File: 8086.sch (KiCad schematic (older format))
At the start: 11 parts

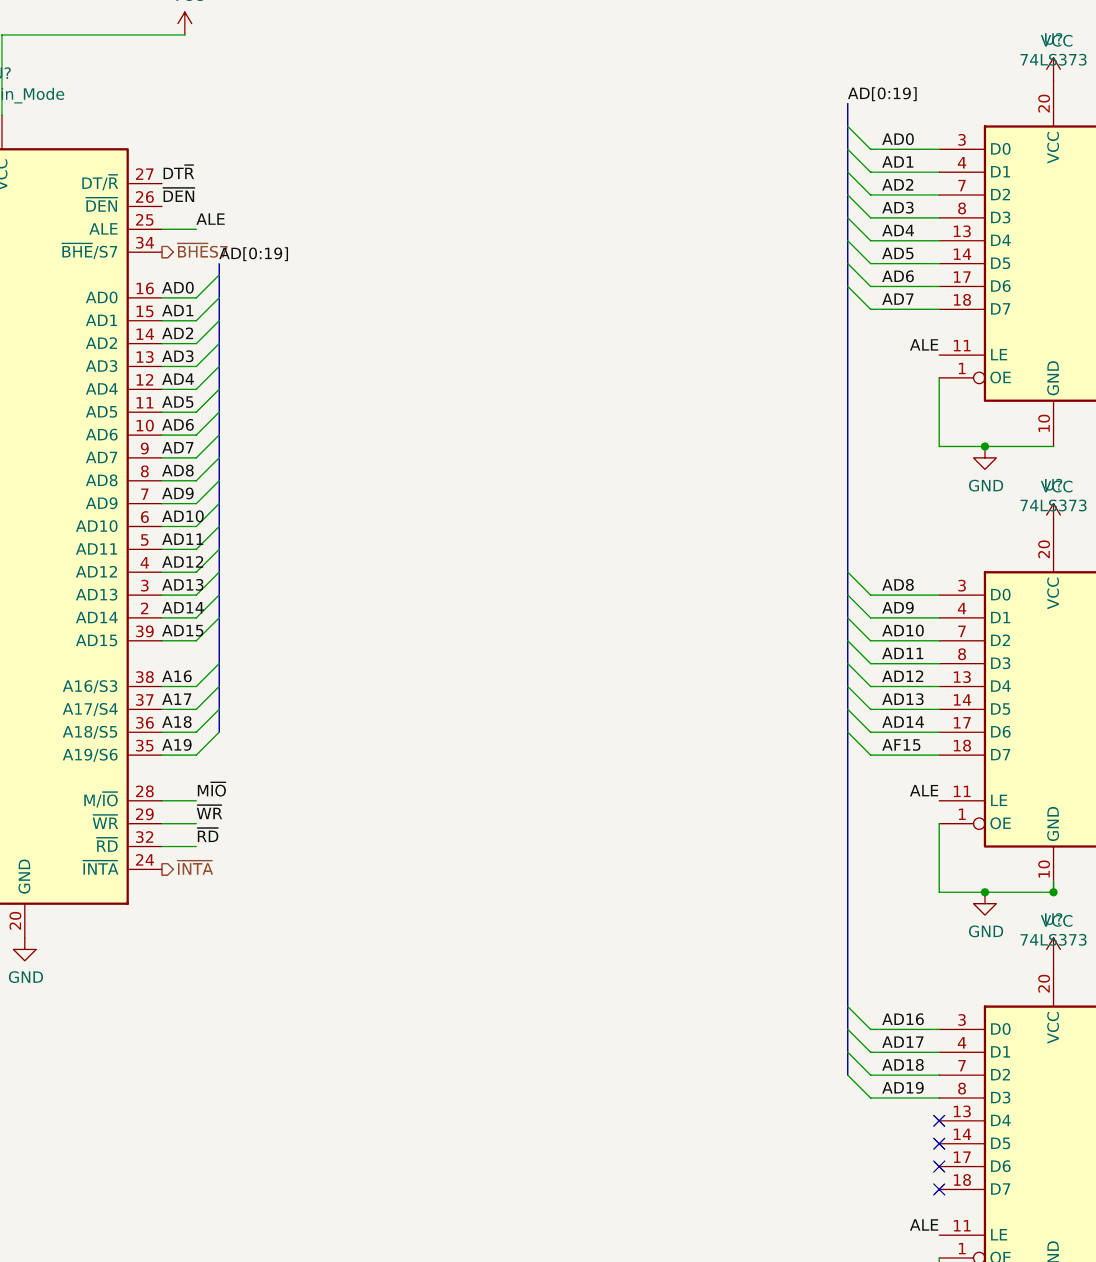
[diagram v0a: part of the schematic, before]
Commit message: Fixed some spelling mistakes
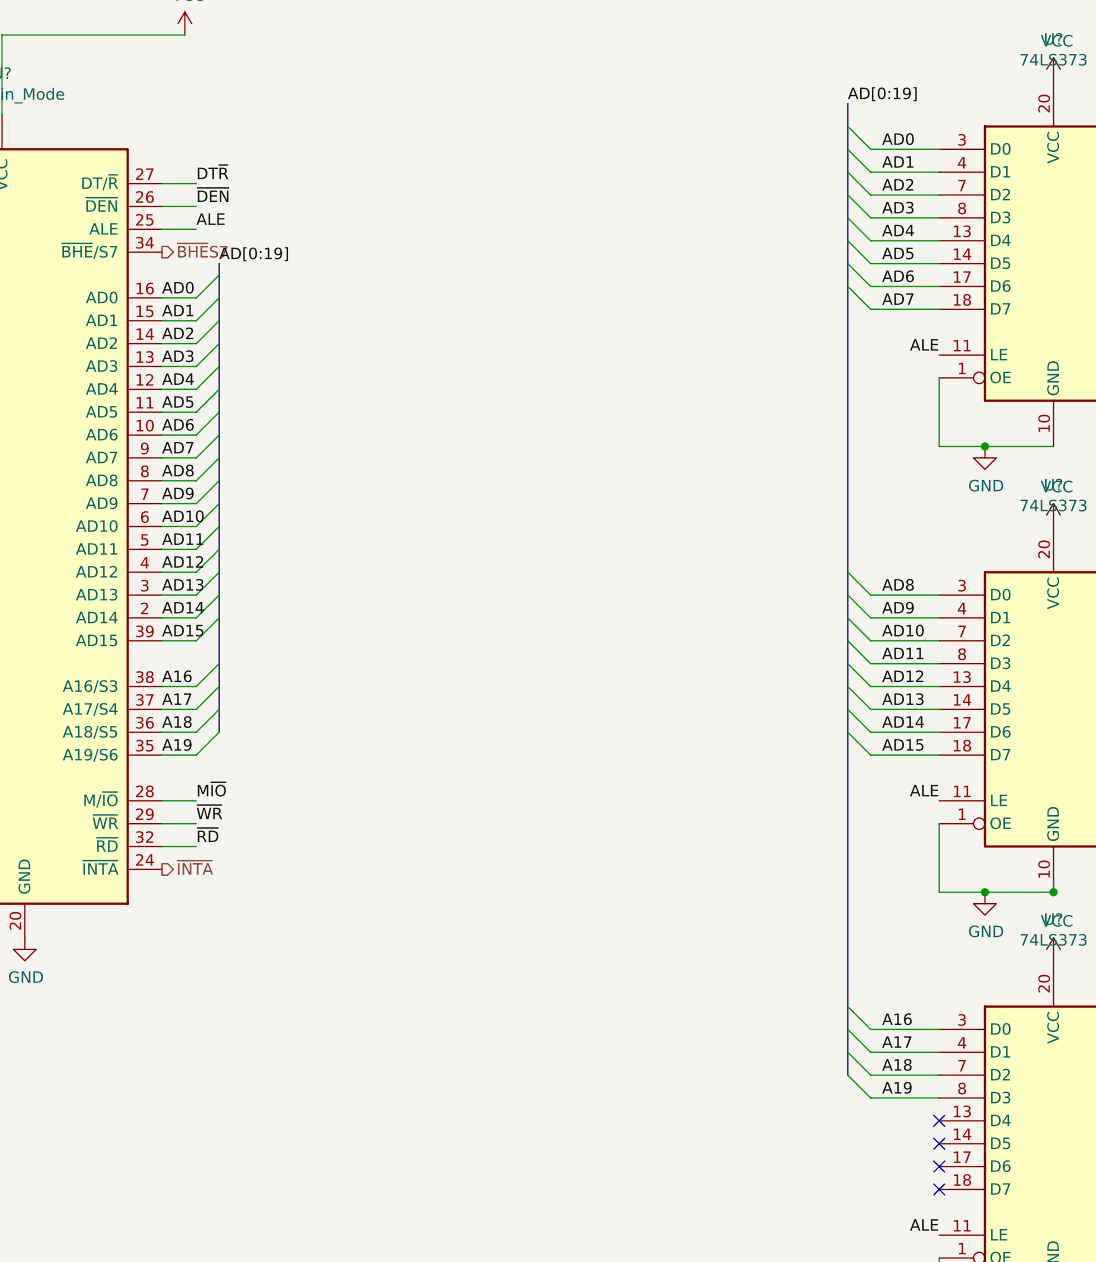
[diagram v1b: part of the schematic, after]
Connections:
- net AD16 is gone; now on net A16: U?.3 (D0)
- net AD17 is gone; now on net A17: U?.4 (D1)
- net AD18 is gone; now on net A18: U?.7 (D2)
- net AD19 is gone; now on net A19: U?.8 (D3)
- net AF15 is gone; now on net AD15: U?.18 (D7)
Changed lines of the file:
@@
 $Descr A4 11693 8268
 encoding utf-8
-Sheet 1 1
+Sheet 1 2
 Title ""
 Date ""
@@
 Wire Wire Line
 	3850 2100 4000 2100
-$Comp
-L MCU_Intel:8086_Min_Mode U?
-U 1 1 60761E58
-P 3150 2700
-F 0 "U?" H 3150 4681 50  0000 C CNN
-F 1 "8086_Min_Mode" H 3150 4590 50  0000 C CNN
-F 2 "Package_DIP:DIP-40_W15.24mm" H 3200 2800 50  0001 C CIN
-F 3 "http://datasheets.chipdb.org/Intel/x86/808x/datashts/8086/231455-006.pdf" H 3150 2750 50  0001 C CNN
-	1    3150 2700
-	1    0    0    -1
-$EndComp
 Wire Wire Line
 	3850 2200 4000 2200
@@
 $EndComp
 Wire Wire Line
-	1850 1900 2450 1900
-Wire Wire Line
 	1850 1550 1850 1900
 Connection ~ 1850 1900
@@
 AD14
 Text Label 7000 3700 0    50   ~ 0
-AF15
+AD15
 Entry Wire Line
 	6850 4800 6950 4900
 Text Label 7000 4900 0    50   ~ 0
-AD16
+A16
 Entry Wire Line
 	6850 4900 6950 5000
 Text Label 7000 5000 0    50   ~ 0
-AD17
+A17
 Entry Wire Line
 	6850 5000 6950 5100
 Text Label 7000 5100 0    50   ~ 0
-AD18
+A18
 Entry Wire Line
 	6850 5100 6950 5200
 Text Label 7000 5200 0    50   ~ 0
-AD19
+A19
 NoConn ~ 7250 5300
 NoConn ~ 7250 5400
@@
 Text Label 9250 2850 0    50   ~ 0
 AD[0:15]
-Text Label 3850 1200 0    50   ~ 0
-DT~R
-Text Label 3850 1300 0    50   ~ 0
+Text Label 4000 1300 0    50   ~ 0
 ~DEN
 Text Label 9650 4050 2    50   ~ 0
@@
 Text HLabel 3850 1500 2    50   Output ~ 0
 ~BHE~S7
-Wire Wire Line
-	2450 1400 2300 1400
 Text Label 2300 1400 2    50   ~ 0
 READY
-Wire Wire Line
-	2300 1600 2450 1600
-Wire Wire Line
-	2450 1200 2300 1200
 $Comp
 L power:GND #PWR?
@@
 	1    0    0    -1
 $EndComp
+Wire Wire Line
+	1850 1900 2450 1900
+Wire Wire Line
+	2300 1600 2450 1600
+Wire Wire Line
+	2450 1400 2300 1400
+Wire Wire Line
+	2450 1200 2300 1200
+$Comp
+L MCU_Intel:8086_Min_Mode U?
+U 1 1 60761E58
+P 3150 2700
+F 0 "U?" H 3150 4681 50  0000 C CNN
+F 1 "8086_Min_Mode" H 3150 4590 50  0000 C CNN
+F 2 "Package_DIP:DIP-40_W15.24mm" H 3200 2800 50  0001 C CIN
+F 3 "http://datasheets.chipdb.org/Intel/x86/808x/datashts/8086/231455-006.pdf" H 3150 2750 50  0001 C CNN
+	1    3150 2700
+	1    0    0    -1
+$EndComp
+Wire Wire Line
+	3850 1200 4000 1200
+Text Label 4000 1200 0    50   ~ 0
+DT~R
+Wire Wire Line
+	3850 1300 4000 1300
+Wire Bus Line
+	9250 2850 9250 5500
 Wire Bus Line
 	6850 850  6850 5100
 Wire Bus Line
 	4100 1550 4100 3600
-Wire Bus Line
-	9250 2850 9250 5500
 $EndSCHEMATC

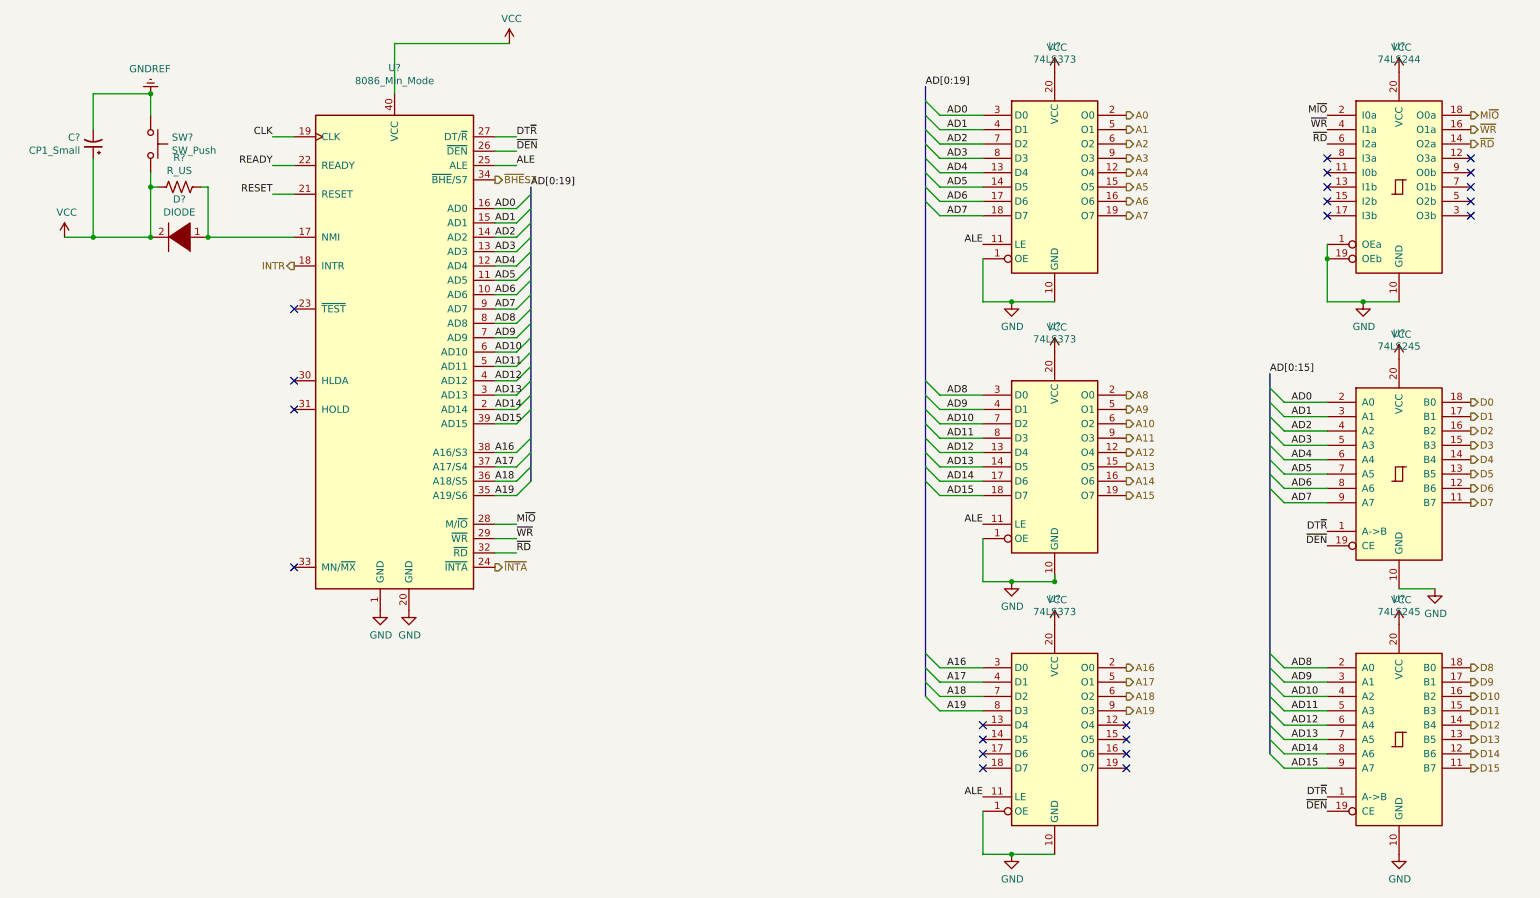
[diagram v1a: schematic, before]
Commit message: Fixed Labels
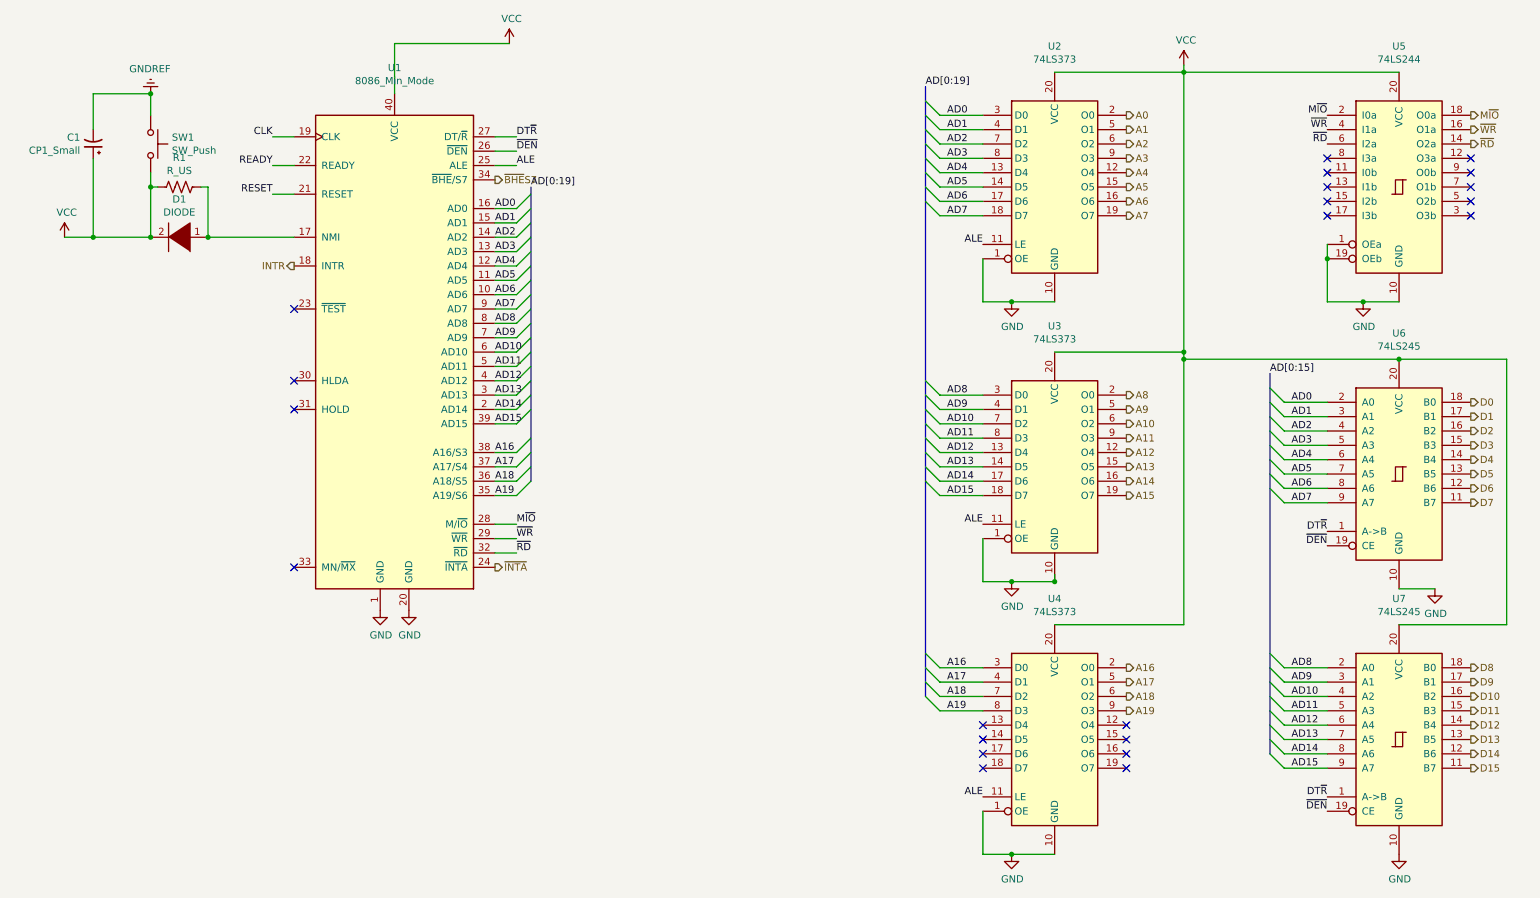
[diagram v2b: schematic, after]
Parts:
- gave numbers to parts that had none: 11
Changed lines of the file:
@@
 $Descr A4 11693 8268
 encoding utf-8
-Sheet 1 2
+Sheet 1 1
 Title ""
 Date ""
@@
 $EndDescr
 $Comp
-L Switch:SW_Push SW?
+L Switch:SW_Push SW1
 U 1 1 607622DA
 P 1450 1250
-F 0 "SW?" V 1404 1398 50  0000 L CNN
+F 0 "SW1" V 1404 1398 50  0000 L CNN
 F 1 "SW_Push" V 1495 1398 50  0000 L CNN
 F 2 "" H 1450 1450 50  0001 C CNN
@@
 	3150 550  3950 550
 $Comp
-L power:VCC #PWR?
+L power:VCC #PWR0101
 U 1 1 60762F72
 P 3950 550
-F 0 "#PWR?" H 3950 400 50  0001 C CNN
+F 0 "#PWR0101" H 3950 400 50  0001 C CNN
 F 1 "VCC" H 3965 723 50  0000 C CNN
 F 2 "" H 3950 550 50  0001 C CNN
@@
 	1450 1550 1500 1550
 $Comp
-L power:VCC #PWR?
+L power:VCC #PWR0102
 U 1 1 60778894
 P 850 1900
-F 0 "#PWR?" H 850 1750 50  0001 C CNN
+F 0 "#PWR0102" H 850 1750 50  0001 C CNN
 F 1 "VCC" H 865 2073 50  0000 C CNN
 F 2 "" H 850 1900 50  0001 C CNN
@@
 $EndComp
 $Comp
-L power:GNDREF #PWR?
+L power:GNDREF #PWR0103
 U 1 1 60779236
 P 1450 900
-F 0 "#PWR?" H 1450 650 50  0001 C CNN
+F 0 "#PWR0103" H 1450 650 50  0001 C CNN
 F 1 "GNDREF" H 1455 727 50  0000 C CNN
 F 2 "" H 1450 900 50  0001 C CNN
@@
 	1050 1350 1050 1900
 $Comp
-L Device:CP1_Small C?
+L Device:CP1_Small C1
 U 1 1 6077E7C3
 P 1050 1250
-F 0 "C?" H 1141 1204 50  0000 L CNN
+F 0 "C1" H 1141 1204 50  0000 L CNN
 F 1 "CP1_Small" H 1141 1295 50  0000 L CNN
 F 2 "" H 1050 1250 50  0001 C CNN
@@
 $EndComp
 $Comp
-L pspice:DIODE D?
+L pspice:DIODE D1
 U 1 1 60781792
 P 1650 1900
-F 0 "D?" H 1650 1635 50  0000 C CNN
+F 0 "D1" H 1650 1635 50  0000 C CNN
 F 1 "DIODE" H 1650 1726 50  0000 C CNN
 F 2 "" H 1650 1900 50  0001 C CNN
@@
 Connection ~ 1050 1900
 $Comp
-L Device:R_US R?
+L Device:R_US R1
 U 1 1 607846D6
 P 1650 1550
-F 0 "R?" V 1445 1550 50  0000 C CNN
+F 0 "R1" V 1445 1550 50  0000 C CNN
 F 1 "R_US" V 1536 1550 50  0000 C CNN
 F 2 "" V 1690 1540 50  0001 C CNN
@@
 A1
 $Comp
-L 74xx:74LS373 U?
+L 74xx:74LS373 U2
 U 1 1 607721F2
 P 7750 1550
-F 0 "U?" H 7750 2531 50  0000 C CNN
+F 0 "U2" H 7750 2531 50  0000 C CNN
 F 1 "74LS373" H 7750 2440 50  0000 C CNN
 F 2 "" H 7750 1550 50  0001 C CNN
@@
 A0
 $Comp
-L 74xx:74LS373 U?
+L 74xx:74LS373 U3
 U 1 1 607A162B
 P 7750 3500
-F 0 "U?" H 7750 4481 50  0000 C CNN
+F 0 "U3" H 7750 4481 50  0000 C CNN
 F 1 "74LS373" H 7750 4390 50  0000 C CNN
 F 2 "" H 7750 3500 50  0001 C CNN
@@
 AD6
 $Comp
-L power:VCC #PWR?
+L power:VCC #PWR0104
 U 1 1 607B535A
-P 7750 750
-F 0 "#PWR?" H 7750 600 50  0001 C CNN
-F 1 "VCC" H 7765 923 50  0000 C CNN
-F 2 "" H 7750 750 50  0001 C CNN
-F 3 "" H 7750 750 50  0001 C CNN
-	1    7750 750
-	1    0    0    -1
-$EndComp
-$Comp
-L power:VCC #PWR?
-U 1 1 607B62FB
-P 7750 2700
-F 0 "#PWR?" H 7750 2550 50  0001 C CNN
-F 1 "VCC" H 7765 2873 50  0000 C CNN
-F 2 "" H 7750 2700 50  0001 C CNN
-F 3 "" H 7750 2700 50  0001 C CNN
-	1    7750 2700
-	1    0    0    -1
-$EndComp
-$Comp
-L power:VCC #PWR?
-U 1 1 607B65E2
-P 7750 4600
-F 0 "#PWR?" H 7750 4450 50  0001 C CNN
-F 1 "VCC" H 7765 4773 50  0000 C CNN
-F 2 "" H 7750 4600 50  0001 C CNN
-F 3 "" H 7750 4600 50  0001 C CNN
-	1    7750 4600
+P 8650 700
+F 0 "#PWR0104" H 8650 550 50  0001 C CNN
+F 1 "VCC" H 8665 873 50  0000 C CNN
+F 2 "" H 8650 700 50  0001 C CNN
+F 3 "" H 8650 700 50  0001 C CNN
+	1    8650 700
 	1    0    0    -1
 $EndComp
@@
 ALE
 $Comp
-L power:GND #PWR?
+L power:GND #PWR0105
 U 1 1 607CF9AE
 P 7450 4300
-F 0 "#PWR?" H 7450 4050 50  0001 C CNN
+F 0 "#PWR0105" H 7450 4050 50  0001 C CNN
 F 1 "GND" H 7455 4127 50  0000 C CNN
 F 2 "" H 7450 4300 50  0001 C CNN
@@
 	7250 2350 7250 2050
 $Comp
-L power:GND #PWR?
+L power:GND #PWR0106
 U 1 1 607D6379
 P 7450 2350
-F 0 "#PWR?" H 7450 2100 50  0001 C CNN
+F 0 "#PWR0106" H 7450 2100 50  0001 C CNN
 F 1 "GND" H 7455 2177 50  0000 C CNN
 F 2 "" H 7450 2350 50  0001 C CNN
@@
 	7250 6200 7250 5900
 $Comp
-L power:GND #PWR?
+L power:GND #PWR0107
 U 1 1 607DB402
 P 7450 6200
-F 0 "#PWR?" H 7450 5950 50  0001 C CNN
+F 0 "#PWR0107" H 7450 5950 50  0001 C CNN
 F 1 "GND" H 7455 6027 50  0000 C CNN
 F 2 "" H 7450 6200 50  0001 C CNN
@@
 	6950 5000 7250 5000
 $Comp
-L 74xx:74LS373 U?
+L 74xx:74LS373 U4
 U 1 1 607A2E66
 P 7750 5400
-F 0 "U?" H 7750 6381 50  0000 C CNN
+F 0 "U4" H 7750 6381 50  0000 C CNN
 F 1 "74LS373" H 7750 6290 50  0000 C CNN
 F 2 "" H 7750 5400 50  0001 C CNN
@@
 A16
 $Comp
-L 74xx:74LS244 U?
+L 74xx:74LS244 U5
 U 1 1 607EFA33
 P 10150 1550
-F 0 "U?" H 10150 2531 50  0000 C CNN
+F 0 "U5" H 10150 2531 50  0000 C CNN
 F 1 "74LS244" H 10150 2440 50  0000 C CNN
 F 2 "" H 10150 1550 50  0001 C CNN
@@
 Connection ~ 9650 2050
 $Comp
-L power:GND #PWR?
+L power:GND #PWR0108
 U 1 1 60803BF6
 P 9900 2350
-F 0 "#PWR?" H 9900 2100 50  0001 C CNN
+F 0 "#PWR0108" H 9900 2100 50  0001 C CNN
 F 1 "GND" H 9905 2177 50  0000 C CNN
 F 2 "" H 9900 2350 50  0001 C CNN
@@
 ~RD
 $Comp
-L power:VCC #PWR?
-U 1 1 6081343C
-P 10150 750
-F 0 "#PWR?" H 10150 600 50  0001 C CNN
-F 1 "VCC" H 10165 923 50  0000 C CNN
-F 2 "" H 10150 750 50  0001 C CNN
-F 3 "" H 10150 750 50  0001 C CNN
-	1    10150 750
-	1    0    0    -1
-$EndComp
-$Comp
-L 74xx:74LS245 U?
+L 74xx:74LS245 U6
 U 1 1 60814065
 P 10150 3550
-F 0 "U?" H 10150 4531 50  0000 C CNN
+F 0 "U6" H 10150 4531 50  0000 C CNN
 F 1 "74LS245" H 10150 4440 50  0000 C CNN
 F 2 "" H 10150 3550 50  0001 C CNN
@@
 $EndComp
 $Comp
-L 74xx:74LS245 U?
+L 74xx:74LS245 U7
 U 1 1 608151DF
 P 10150 5400
-F 0 "U?" H 10150 6381 50  0000 C CNN
+F 0 "U7" H 10150 6381 50  0000 C CNN
 F 1 "74LS245" H 10150 6290 50  0000 C CNN
 F 2 "" H 10150 5400 50  0001 C CNN
@@
 Text Label 9650 5900 2    50   ~ 0
 ~DEN
-$Comp
-L power:VCC #PWR?
-U 1 1 6083AE50
-P 10150 2750
-F 0 "#PWR?" H 10150 2600 50  0001 C CNN
-F 1 "VCC" H 10165 2923 50  0000 C CNN
-F 2 "" H 10150 2750 50  0001 C CNN
-F 3 "" H 10150 2750 50  0001 C CNN
-	1    10150 2750
-	1    0    0    -1
-$EndComp
-$Comp
-L power:VCC #PWR?
-U 1 1 6083B498
-P 10150 4600
-F 0 "#PWR?" H 10150 4450 50  0001 C CNN
-F 1 "VCC" H 10165 4773 50  0000 C CNN
-F 2 "" H 10150 4600 50  0001 C CNN
-F 3 "" H 10150 4600 50  0001 C CNN
-	1    10150 4600
-	1    0    0    -1
-$EndComp
 Wire Wire Line
 	10150 4350 10400 4350
 $Comp
-L power:GND #PWR?
+L power:GND #PWR0109
 U 1 1 6083EB10
 P 10150 6200
-F 0 "#PWR?" H 10150 5950 50  0001 C CNN
+F 0 "#PWR0109" H 10150 5950 50  0001 C CNN
 F 1 "GND" H 10155 6027 50  0000 C CNN
 F 2 "" H 10150 6200 50  0001 C CNN
@@
 $EndComp
 $Comp
-L power:GND #PWR?
+L power:GND #PWR0110
 U 1 1 6083F138
 P 10400 4350
-F 0 "#PWR?" H 10400 4100 50  0001 C CNN
+F 0 "#PWR0110" H 10400 4100 50  0001 C CNN
 F 1 "GND" H 10405 4177 50  0000 C CNN
 F 2 "" H 10400 4350 50  0001 C CNN
@@
 READY
 $Comp
-L power:GND #PWR?
+L power:GND #PWR0111
 U 1 1 6085F789
 P 3050 4500
-F 0 "#PWR?" H 3050 4250 50  0001 C CNN
+F 0 "#PWR0111" H 3050 4250 50  0001 C CNN
 F 1 "GND" H 3055 4327 50  0000 C CNN
 F 2 "" H 3050 4500 50  0001 C CNN
@@
 $EndComp
 $Comp
-L power:GND #PWR?
+L power:GND #PWR0112
 U 1 1 60860099
 P 3250 4500
-F 0 "#PWR?" H 3250 4250 50  0001 C CNN
+F 0 "#PWR0112" H 3250 4250 50  0001 C CNN
 F 1 "GND" H 3255 4327 50  0000 C CNN
 F 2 "" H 3250 4500 50  0001 C CNN
@@
 	2450 1200 2300 1200
 $Comp
-L MCU_Intel:8086_Min_Mode U?
+L MCU_Intel:8086_Min_Mode U1
 U 1 1 60761E58
 P 3150 2700
-F 0 "U?" H 3150 4681 50  0000 C CNN
+F 0 "U1" H 3150 4681 50  0000 C CNN
 F 1 "8086_Min_Mode" H 3150 4590 50  0000 C CNN
 F 2 "Package_DIP:DIP-40_W15.24mm" H 3200 2800 50  0001 C CIN
@@
 Wire Wire Line
 	3850 1300 4000 1300
+Wire Wire Line
+	7750 750  8650 750
+Wire Wire Line
+	8650 750  8650 700
+Wire Wire Line
+	7750 4600 8650 4600
+Wire Wire Line
+	8650 4600 8650 2750
+Connection ~ 8650 750
+Wire Wire Line
+	7750 2700 8650 2700
+Connection ~ 8650 2700
+Wire Wire Line
+	8650 2700 8650 750
+Wire Wire Line
+	10150 750  8650 750
+Wire Wire Line
+	10150 2750 8650 2750
+Connection ~ 8650 2750
+Wire Wire Line
+	8650 2750 8650 2700
+Wire Wire Line
+	10150 4600 10900 4600
+Wire Wire Line
+	10900 4600 10900 2750
+Wire Wire Line
+	10900 2750 10150 2750
 Wire Bus Line
 	9250 2850 9250 5500
@@
 Wire Bus Line
 	4100 1550 4100 3600
+Connection ~ 10150 2750
 $EndSCHEMATC
